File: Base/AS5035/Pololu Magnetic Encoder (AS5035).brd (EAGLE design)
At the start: 17.8 x 11.7 mm, 9 parts, among them U1 AS5035

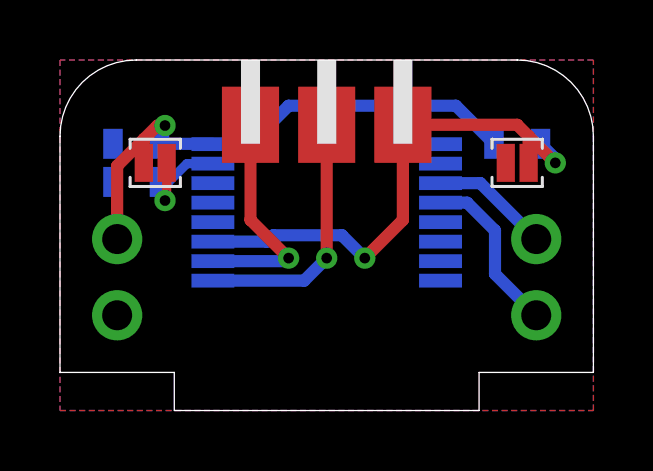
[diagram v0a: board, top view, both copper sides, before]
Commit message: Cleaned up AS5035 based Magnetic Encoder. Added Silkscreen adn removed SPI components.
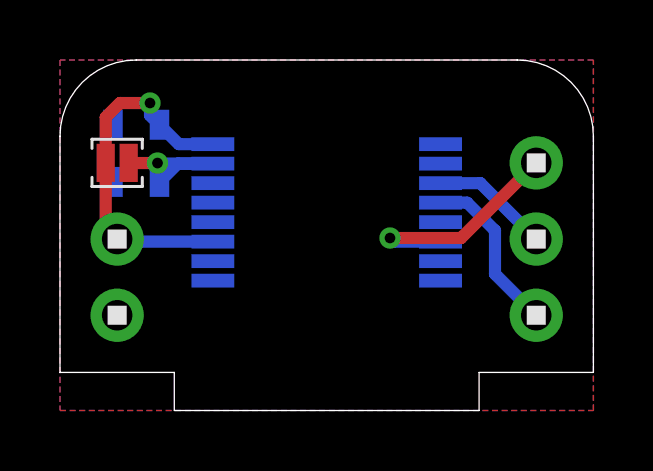
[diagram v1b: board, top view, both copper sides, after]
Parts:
- removed J2: (no value), .solderjumper:2.LRG.PASTE
- removed JP1, JP2: (no value), microbuilder:1X02_ROUND
- removed R1: 100k, .standardparts:0603
- removed U$9: 1X3.SIDE, .standardheaders:1X3.SIDE
- added U$4: 1X3, headers(.1in):1X3
- added U$5: 1X2, headers(.1in):1X2
- moved J1 1.27 mm to (1.91, 8.26)
- moved C1 0.63 mm to (2.54, 9.53)
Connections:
- removed net !CS: J2.2, R1.2, U$9.3, U1.11
- removed net CLK: U$9.1, U1.10
- removed net DO: U$9.2, U1.9
- new net NDX: U$4.1, U1.6
- net A: now also U$4.2; no longer JP2.2
- net B: now also U$4.3; no longer JP2.1
- net GND: now also U$5.2; no longer J2.1, JP1.1
- net VIN: now also U$5.1, U1.11; no longer JP1.2, R1.1
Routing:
- net !CS: track 17.8 -> 0.00 mm, vias 2 -> 0
- net DO: track 8.55 -> 0.00 mm, vias 1 -> 0
- net CLK: track 8.17 -> 0.00 mm, vias 1 -> 0
- net NDX: track 0.00 -> 7.65 mm, vias 0 -> 1
- net VIN: track 18.3 -> 12.0 mm
- net N$4: track 4.01 -> 4.85 mm
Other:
- board text added: "A"
- board text added: "AnomalousMaker.com"
- board text added: "B"
- board text added: "GND"
- board text added: "INDEX"
- board text added: "Magnetic QEI Encoder"
- board text added: "Vin"
- board text removed: "!CS"
- board text removed: "!SPI"
- board text removed: "CLK"
- board text removed: "DO"
- board text removed: "innovativemaker.com"
